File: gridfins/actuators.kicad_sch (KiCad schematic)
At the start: 9 parts

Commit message: update 2
Renamed repeated resistor names. Changed typo in buck - removing the 442k resistor actually changes Vout to 7.4V not 8.4! We need 7.4V for servos.
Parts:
- gave numbers to parts that had none: 8
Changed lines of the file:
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@@
 		(dnp no)
 		(fields_autoplaced yes)
-		(property "Reference" "R?"
+		(property "Reference" "R26"
 			(at 144.78 96.52 90)
 			(effects
@@
 			(project "RicardoTemplate"
 				(path "/7db990e4-92e1-4f99-b4d2-435bbec1ba83/4a649bbd-9e5c-4376-be49-6107979e6dfc"
-					(reference "R?")
+					(reference "R26")
 					(unit 1)
 				)
@@
 		(on_board yes)
 		(dnp no)
-		(property "Reference" "D?"
+		(property "Reference" "D5"
 			(at 114.046 89.408 0)
 			(effects
@@
 			(project "RicardoTemplate"
 				(path "/7db990e4-92e1-4f99-b4d2-435bbec1ba83/4a649bbd-9e5c-4376-be49-6107979e6dfc"
-					(reference "D?")
+					(reference "D5")
 					(unit 1)
 				)
@@
 		(on_board yes)
 		(dnp no)
-		(property "Reference" "#PWR?"
+		(property "Reference" "#PWR0101"
 			(at 111.76 105.41 0)
 			(effects
@@
 			(project "RicardoTemplate"
 				(path "/7db990e4-92e1-4f99-b4d2-435bbec1ba83/4a649bbd-9e5c-4376-be49-6107979e6dfc"
-					(reference "#PWR?")
+					(reference "#PWR0101")
 					(unit 1)
 				)
@@
 		(on_board yes)
 		(dnp no)
-		(property "Reference" "#PWR?"
+		(property "Reference" "#PWR0104"
 			(at 135.89 92.71 0)
 			(effects
@@
 			(project "RicardoTemplate"
 				(path "/7db990e4-92e1-4f99-b4d2-435bbec1ba83/4a649bbd-9e5c-4376-be49-6107979e6dfc"
-					(reference "#PWR?")
+					(reference "#PWR0104")
 					(unit 1)
 				)
@@
 		(on_board yes)
 		(dnp no)
-		(property "Reference" "J?"
+		(property "Reference" "J5"
 			(at 152.4 114.3 0)
 			(effects
@@
 			(project "RicardoTemplate"
 				(path "/7db990e4-92e1-4f99-b4d2-435bbec1ba83/4a649bbd-9e5c-4376-be49-6107979e6dfc"
-					(reference "J?")
+					(reference "J5")
 					(unit 1)
 				)
@@
 		(on_board yes)
 		(dnp no)
-		(property "Reference" "#PWR?"
+		(property "Reference" "#PWR0106"
 			(at 138.43 124.46 0)
 			(effects
@@
 			(project "RicardoTemplate"
 				(path "/7db990e4-92e1-4f99-b4d2-435bbec1ba83/4a649bbd-9e5c-4376-be49-6107979e6dfc"
-					(reference "#PWR?")
+					(reference "#PWR0106")
 					(unit 1)
 				)
@@
 		(on_board yes)
 		(dnp no)
-		(property "Reference" "#PWR?"
+		(property "Reference" "#PWR0108"
 			(at 143.51 106.68 0)
 			(effects
@@
 			(project "RicardoTemplate"
 				(path "/7db990e4-92e1-4f99-b4d2-435bbec1ba83/4a649bbd-9e5c-4376-be49-6107979e6dfc"
-					(reference "#PWR?")
+					(reference "#PWR0108")
 					(unit 1)
 				)
@@
 		(on_board yes)
 		(dnp no)
-		(property "Reference" "#PWR?"
+		(property "Reference" "#PWR0107"
 			(at 143.51 91.44 0)
 			(effects
@@
 			(project "RicardoTemplate"
 				(path "/7db990e4-92e1-4f99-b4d2-435bbec1ba83/4a649bbd-9e5c-4376-be49-6107979e6dfc"
-					(reference "#PWR?")
+					(reference "#PWR0107")
 					(unit 1)
 				)
@@
 		(on_board yes)
 		(dnp no)
-		(property "Reference" "J?"
+		(property "Reference" "J3"
 			(at 152.4 82.55 0)
 			(effects
@@
 			(project "RicardoTemplate"
 				(path "/7db990e4-92e1-4f99-b4d2-435bbec1ba83/4a649bbd-9e5c-4376-be49-6107979e6dfc"
-					(reference "J?")
+					(reference "J3")
 					(unit 1)
 				)
@@
 		(on_board yes)
 		(dnp no)
-		(property "Reference" "J?"
+		(property "Reference" "J4"
 			(at 152.4 97.79 0)
 			(effects
@@
 			(project "RicardoTemplate"
 				(path "/7db990e4-92e1-4f99-b4d2-435bbec1ba83/4a649bbd-9e5c-4376-be49-6107979e6dfc"
-					(reference "J?")
+					(reference "J4")
 					(unit 1)
 				)
@@
 		(on_board yes)
 		(dnp no)
-		(property "Reference" "D?"
+		(property "Reference" "D4"
 			(at 102.108 92.71 0)
 			(effects
@@
 			(project "RicardoTemplate"
 				(path "/7db990e4-92e1-4f99-b4d2-435bbec1ba83/4a649bbd-9e5c-4376-be49-6107979e6dfc"
-					(reference "D?")
+					(reference "D4")
 					(unit 1)
 				)
@@
 		(dnp no)
 		(fields_autoplaced yes)
-		(property "Reference" "R?"
+		(property "Reference" "R27"
 			(at 144.78 113.03 90)
 			(effects
@@
 			(project "RicardoTemplate"
 				(path "/7db990e4-92e1-4f99-b4d2-435bbec1ba83/4a649bbd-9e5c-4376-be49-6107979e6dfc"
-					(reference "R?")
+					(reference "R27")
 					(unit 1)
 				)
@@
 		(on_board yes)
 		(dnp no)
-		(property "Reference" "#PWR?"
+		(property "Reference" "#PWR0103"
 			(at 143.51 123.19 0)
 			(effects
@@
 			(project "RicardoTemplate"
 				(path "/7db990e4-92e1-4f99-b4d2-435bbec1ba83/4a649bbd-9e5c-4376-be49-6107979e6dfc"
-					(reference "#PWR?")
+					(reference "#PWR0103")
 					(unit 1)
 				)
@@
 		(on_board yes)
 		(dnp no)
-		(property "Reference" "R?"
+		(property "Reference" "R25"
 			(at 144.526 81.534 90)
 			(effects
@@
 			(project "RicardoTemplate"
 				(path "/7db990e4-92e1-4f99-b4d2-435bbec1ba83/4a649bbd-9e5c-4376-be49-6107979e6dfc"
-					(reference "R?")
+					(reference "R25")
 					(unit 1)
 				)
@@
 		(on_board yes)
 		(dnp no)
-		(property "Reference" "#PWR?"
+		(property "Reference" "#PWR0102"
 			(at 104.14 105.41 0)
 			(effects
@@
 			(project "RicardoTemplate"
 				(path "/7db990e4-92e1-4f99-b4d2-435bbec1ba83/4a649bbd-9e5c-4376-be49-6107979e6dfc"
-					(reference "#PWR?")
+					(reference "#PWR0102")
 					(unit 1)
 				)
@@
 		(on_board yes)
 		(dnp no)
-		(property "Reference" "#PWR?"
+		(property "Reference" "#PWR0105"
 			(at 138.43 107.95 0)
 			(effects
@@
 			(project "RicardoTemplate"
 				(path "/7db990e4-92e1-4f99-b4d2-435bbec1ba83/4a649bbd-9e5c-4376-be49-6107979e6dfc"
-					(reference "#PWR?")
-					(unit 1)
-				)
+					(reference "#PWR0105")
+					(unit 1)
+				)

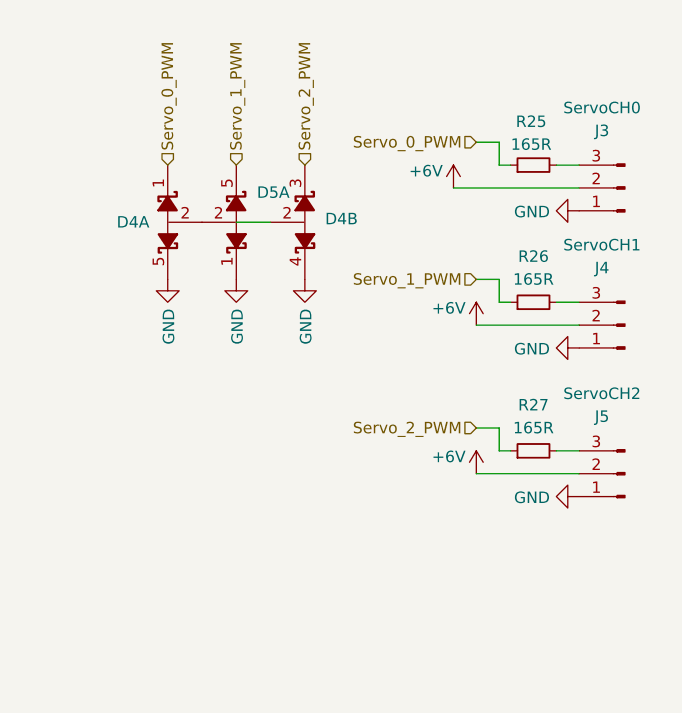
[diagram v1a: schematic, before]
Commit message: update 3
added tvs diode chip module for 3rd servo
added net connection to actuators sheet
changed 6 to 7.4 label
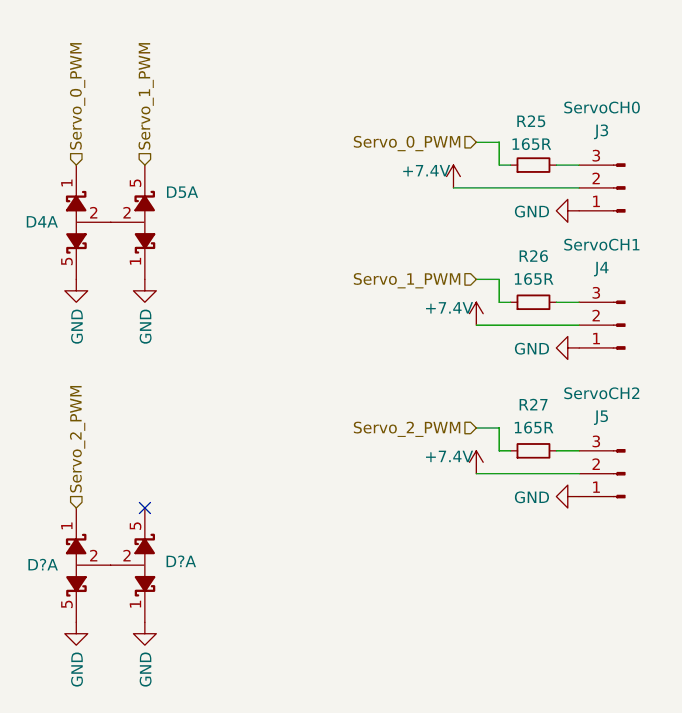
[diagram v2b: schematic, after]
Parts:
- removed unit 2 of D4
- added D? (x2): ~, Package_TO_SOT_SMD:SOT-353_SC-70-5, symbol iclr:CPDV5-3V3UP
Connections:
- net GND: now also D?.1, D?.5
- net Servo_2_PWM: now also D?.1
- net +6V renamed +7.4V
- new net: D?.2, D?.2
- no-connect marks 0 -> 1
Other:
- moved on the sheet: D4A, D5A

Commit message: Update with Inertial Measurement Unit
cloned IMU from pickle rick.
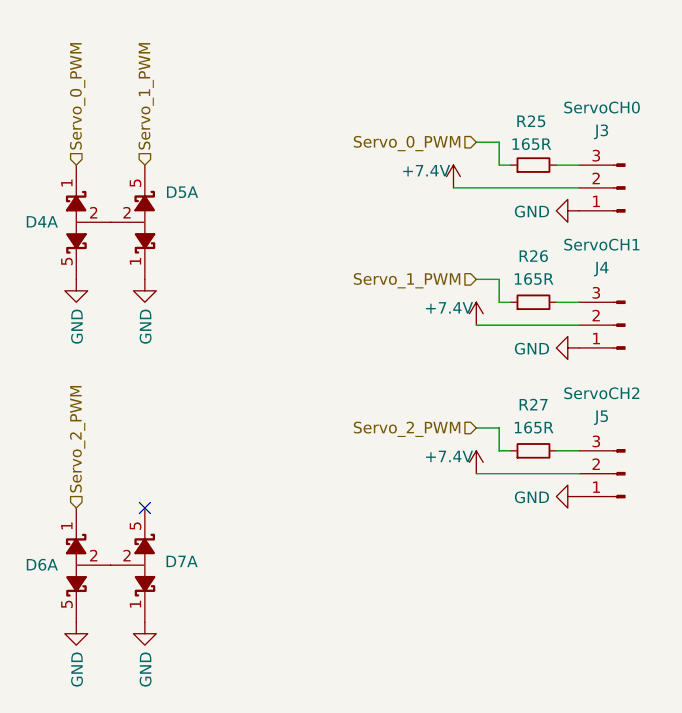
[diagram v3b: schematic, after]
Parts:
- gave numbers to parts that had none: 2
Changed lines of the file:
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@@
 		(on_board yes)
 		(dnp no)
-		(property "Reference" "#PWR?"
+		(property "Reference" "#PWR0110"
 			(at 93.98 143.51 0)
 			(effects
@@
 			(project "gridfins"
 				(path "/7db990e4-92e1-4f99-b4d2-435bbec1ba83/4a649bbd-9e5c-4376-be49-6107979e6dfc"
-					(reference "#PWR?")
+					(reference "#PWR0110")
 					(unit 1)
 				)
@@
 		(on_board yes)
 		(dnp no)
-		(property "Reference" "D?"
+		(property "Reference" "D6"
 			(at 91.948 130.81 0)
 			(effects
@@
 			(project "gridfins"
 				(path "/7db990e4-92e1-4f99-b4d2-435bbec1ba83/4a649bbd-9e5c-4376-be49-6107979e6dfc"
-					(reference "D?")
+					(reference "D6")
 					(unit 1)
 				)
@@
 		(on_board yes)
 		(dnp no)
-		(property "Reference" "#PWR?"
+		(property "Reference" "#PWR0109"
 			(at 101.6 143.51 0)
 			(effects
@@
 			(project "gridfins"
 				(path "/7db990e4-92e1-4f99-b4d2-435bbec1ba83/4a649bbd-9e5c-4376-be49-6107979e6dfc"
-					(reference "#PWR?")
+					(reference "#PWR0109")
 					(unit 1)
 				)
@@
 		(dnp no)
 		(fields_autoplaced yes)
-		(property "Reference" "D?"
+		(property "Reference" "D7"
 			(at 103.8417 130.4449 0)
 			(effects
@@
 			(project "gridfins"
 				(path "/7db990e4-92e1-4f99-b4d2-435bbec1ba83/4a649bbd-9e5c-4376-be49-6107979e6dfc"
-					(reference "D?")
-					(unit 1)
-				)
+					(reference "D7")
+					(unit 1)
+				)

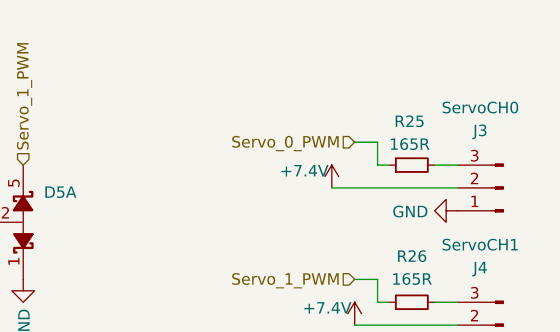
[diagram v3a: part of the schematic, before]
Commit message: SD card, linear actuator encoders
Imported microSD reader from Stark

Added pin connectors and SPI routes for AS5048 magnetic rotary encoder to be used with the linear actuator/brushed motor

Added test pads for SD reader and encoder chip select
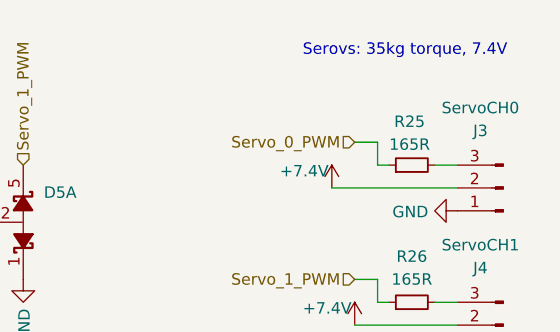
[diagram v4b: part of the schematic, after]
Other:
- note added: "Serovs: 35kg torque, 7.4V"
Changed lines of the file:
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@@
 	(generator_version "9.0")
 	(paper "A4")
+	(text "Serovs: 35kg torque, 7.4V\n"
+		(exclude_from_sim no)
+		(at 144.018 73.66 0)
+		(effects
+			(font
+				(size 1.27 1.27)
+			)
+		)
+	)
 	(no_connect
 		(at 101.6 124.46)
